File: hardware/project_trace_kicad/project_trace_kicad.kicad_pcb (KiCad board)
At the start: 4 copper layers, 100 x 100 mm, 77 parts, among them J204 Screw_Terminal_01x04, J205 Conn_Coaxial, J503 Screw_Terminal_01x04, U1 OPA2837IRUNT, U2 OPA2837IRUNT, U202 AQW280SX, U203 AQW282SX, U204 TS5A23159DGS, U206 TLE2426xLP, U301 LM358, U302 ADS1602, U304 MCP6499T, U306 LM4040DBZ-2.5, U307 LM4040DBZ-4.1, U501 UA78M33QDCYRQ1, U502 UA78M05QDCYRQ1

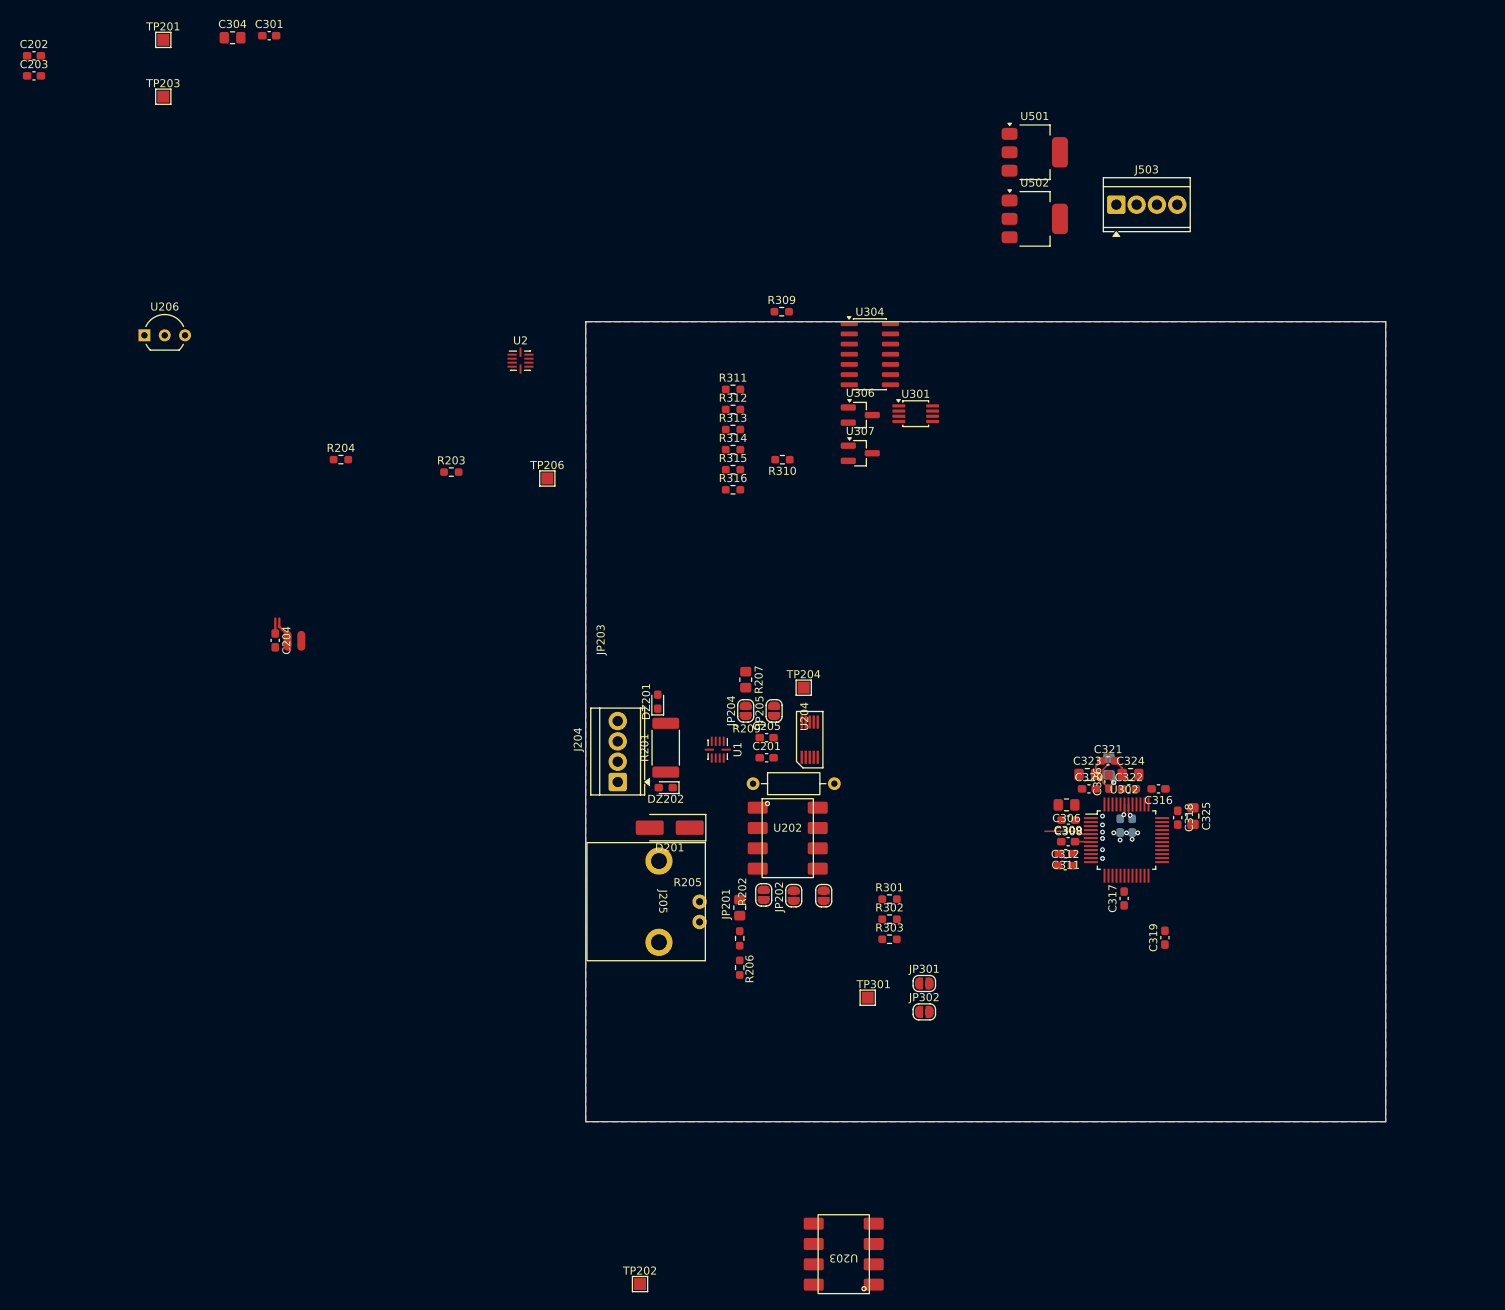
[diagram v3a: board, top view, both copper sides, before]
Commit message: Work on PCB, Fix bugs, Improve noise performance
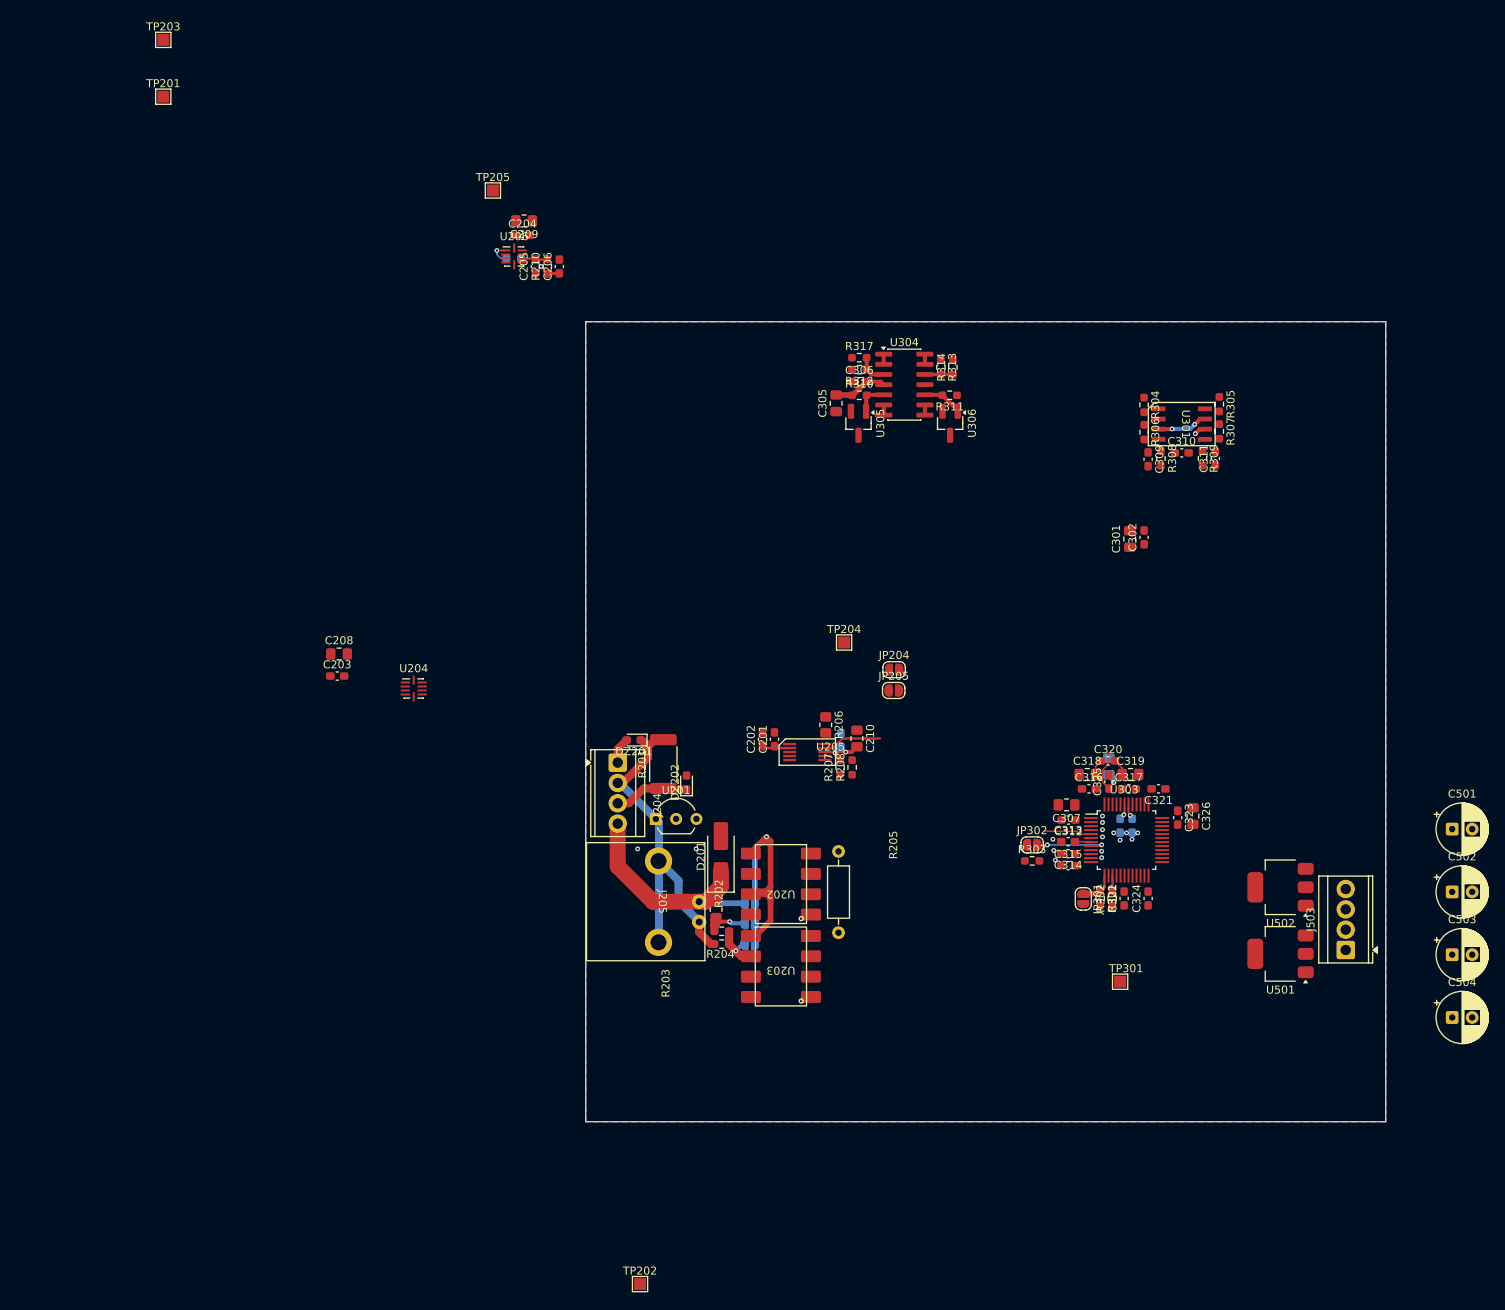
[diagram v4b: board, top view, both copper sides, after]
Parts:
- removed the R314 at (118.4, 66.0)
- removed R315: 15k, Resistor_SMD:R_0603_1608Metric_Pad0.98x0.95mm_HandSolder
- added C205: 300p, Capacitor_SMD:C_0603_1608Metric_Pad1.08x0.95mm_HandSolder, F.Cu at (93.7, 43.1)
- added C206: 680p, Capacitor_SMD:C_0603_1608Metric_Pad1.08x0.95mm_HandSolder, F.Cu at (96.7, 43.1)
- added C208: 10u, Capacitor_SMD:C_0805_2012Metric_Pad1.18x1.45mm_HandSolder, F.Cu at (69.2, 91.5)
- added C209: 10u, Capacitor_SMD:C_0805_2012Metric_Pad1.18x1.45mm_HandSolder, F.Cu at (92.3, 37.4)
- added C210: 10u, Capacitor_SMD:C_0805_2012Metric_Pad1.18x1.45mm_HandSolder, F.Cu at (133.9, 102.1)
- added C302: 100n, Capacitor_SMD:C_0603_1608Metric_Pad1.08x0.95mm_HandSolder, F.Cu at (169.8, 77.0)
- added C306: 100n, Capacitor_SMD:C_0603_1608Metric_Pad1.08x0.95mm_HandSolder, F.Cu at (134.2, 57.5)
- added C309: 100p, Capacitor_SMD:C_0603_1608Metric_Pad1.08x0.95mm_HandSolder, F.Cu at (170.3, 67.2)
- added C310: 100p, Capacitor_SMD:C_0603_1608Metric_Pad1.08x0.95mm_HandSolder, F.Cu at (174.5, 66.4)
- added C311: 100p, Capacitor_SMD:C_0603_1608Metric_Pad1.08x0.95mm_HandSolder, F.Cu at (178.7, 67.1)
- added C501: 100u, Capacitor_THT:CP_Radial_D6.3mm_P2.50mm, F.Cu at (208.3, 113.4)
- added C502: 100u, Capacitor_THT:CP_Radial_D6.3mm_P2.50mm, F.Cu at (208.3, 121.3)
- added C503: 100u, Capacitor_THT:CP_Radial_D6.3mm_P2.50mm, F.Cu at (208.3, 129.1)
- added C504: 100u, Capacitor_THT:CP_Radial_D6.3mm_P2.50mm, F.Cu at (208.3, 137.0)
- added R209: 111R, Resistor_SMD:R_0603_1608Metric_Pad0.98x0.95mm_HandSolder, B.Cu at (91.0, 42.1)
- added R210: 193R, Resistor_SMD:R_0603_1608Metric_Pad0.98x0.95mm_HandSolder, F.Cu at (95.2, 43.1)
- added R304: 330R, Resistor_SMD:R_0603_1608Metric_Pad0.98x0.95mm_HandSolder, F.Cu at (169.8, 60.4)
- added R305: 330R, Resistor_SMD:R_0603_1608Metric_Pad0.98x0.95mm_HandSolder, F.Cu at (179.2, 60.3)
- added R306: 1k, Resistor_SMD:R_0603_1608Metric_Pad0.98x0.95mm_HandSolder, F.Cu at (169.8, 63.8)
- added R307: 1k, Resistor_SMD:R_0603_1608Metric_Pad0.98x0.95mm_HandSolder, F.Cu at (179.2, 63.7)
- added R308: 24R9, Resistor_SMD:R_0603_1608Metric_Pad0.98x0.95mm_HandSolder, F.Cu at (171.9, 67.1)
- added R309: 24R9, Resistor_SMD:R_0603_1608Metric_Pad0.98x0.95mm_HandSolder, F.Cu at (177.1, 67.1)
- C207: renamed from C204; moved to B.Cu
- C301: value 100n -> 10u; footprint Capacitor_SMD:C_0603_1608Metric_Pad1.08x0.95mm_HandSolder -> Capacitor_SMD:C_0805_2012Metric_Pad1.18x1.45mm_HandSolder
- JP201, JP202, JP203: moved to B.Cu
- R207: renamed from R203; value 10k -> 1k
- R208: renamed from R204; value 89k8 -> 8k98
- U301: value LM358 -> THS4131IDR; footprint Package_SO:MSOP-8_3x3mm_P0.65mm -> ProjectTraceFootprints:SOIC8 - D0008A - THS4131IDR
- moved C301 124.6 mm to (168.0, 77.2), turned to 90 degrees
- moved U501 104.8 mm to (186.8, 129.0), turned to 180 degrees
- moved J503 97.5 mm to (195.0, 128.5), turned to 90 degrees
- moved U502 89.0 mm to (186.8, 120.7), turned to 180 degrees
- moved C305 88.2 mm to (131.3, 60.2), turned to 90 degrees
- moved U201 88.0 mm to (108.8, 112.2)
- moved C203 84.1 mm to (68.9, 94.3)
- moved R208 74.6 mm to (133.3, 105.7), turned to 90 degrees
- moved C207 71.8 mm to (131.9, 102.3), turned to 90 degrees
- moved C204 65.1 mm to (92.1, 39.2)
- moved R207 61.0 mm to (131.8, 105.7), turned to 90 degrees
- moved U204 38.8 mm to (78.5, 95.8), turned to 0 degrees
- moved U203 36.8 mm to (124.4, 130.6)
- moved TP205 36.6 mm to (88.4, 33.6)
- moved U301 33.3 mm to (174.5, 62.8)
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- renumbered C205 to C201, C201 to C202, C202 to C204, C303 to C304, C304 to C305, C306 to C307, C307 to C308, C308 to C312, C309 to C313, C311 to C314, C312 to C315, C320 to C316, C322 to C317, C323 to C318, C324 to C319, C321 to C320, C316 to C321, C317 to C322, C318 to C323, C319 to C324, C326 to C325, C325 to C326, JP302 to JP301, JP301 to JP302, R205 to R203, R206 to R204, R209 to R205, R207 to R206, R303 to R301, R301 to R302, R302 to R303, R309 to R310, R310 to R311, R313 to R312, R312 to R313, R311 to R314, R316 to R317, TP203 to TP201, TP201 to TP203, TP206 to TP205, U206 to U201, U1 to U204, U204 to U205, U2 to U206, U302 to U303, U306 to U305, U307 to U306
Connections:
- J204 pad 1: /Inputs/Voltmeter.In -> GND
- J204 pad 2: /Inputs/Ammeter.In -> VCOM
- J204 pad 3: VCOM -> /Inputs/Ammeter.In
- J204 pad 4: GND -> /Inputs/Voltmeter.In
- R311 pad 2: Net-(U301A-+) -> Net-(U304C-+)
- U202 pad 2: /Inputs/0dBAtten.~{EN} -> /Inputs/-20dBAtten.~{EN}
- U202 pad 4: /Inputs/-20dBAtten.~{EN} -> /Inputs/0dBAtten.~{EN}
- U202 pad 6: /Inputs/Attten.20dB -> /Inputs/Voltmeter.In
- U202 pad 8: /Inputs/Voltmeter.In -> /Inputs/Attten.20dB
- U203 pad 1: Net-(U202A-P1) -> GND
- U203 pad 2: /Inputs/-40dBAtten.~{EN} -> GND
- U203 pad 3: GND -> Net-(U202A-P1)
- U203 pad 4: GND -> /Inputs/-40dBAtten.~{EN}
- U203 pad 5: GND -> Net-(JP201-B)
- U203 pad 6: GND -> /Inputs/Attten.40dB
- U203 pad 7: Net-(JP201-B) -> GND
- U203 pad 8: /Inputs/Attten.40dB -> GND
- U301 pad 1: 4V1 -> Net-(R304-Pad2)
- U301 pad 2: 4V1 -> +2V5
- U301 pad 3: Net-(U301A-+) -> +5V
- U301 pad 4: GND -> Net-(R306-Pad2)
- U301 pad 5: GND -> Net-(R307-Pad2)
- U301 pad 7: unconnected-(U301-Pad7) -> +5V
- U301 pad 8: +5V -> Net-(R305-Pad2)
- U303 pad 4: GND -> Net-(U303A-AINN)
- U303 pad 5: /ADC/Signal.In -> Net-(U303A-AINP)
- U304 pad 8: +1V5 -> 4V1
- U304 pad 9: +1V5 -> 4V1
- U306 pad 1: Net-(U301A-+) -> Net-(U304C-+)
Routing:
- net VCOM: track 0.00 -> 46.3 mm
- net Net-(JP201-B): track 0.00 -> 36.7 mm, vias 0 -> 1
- net /Inputs/Voltmeter.In: track 0.00 -> 30.7 mm
- net +5V: track 5.33 -> 22.7 mm, vias 1 -> 5
- net Net-(JP302-B): track 0.00 -> 9.46 mm, vias 0 -> 2
- net /Inputs/Ammeter.In: track 0.00 -> 9.26 mm
- net /Inputs/Attten.40dB: track 0.00 -> 6.41 mm, vias 0 -> 1
- net /Inputs/Attten.20dB: track 0.00 -> 6.19 mm, vias 0 -> 1
- net Net-(U303A-AINP): track 0.00 -> 5.89 mm
- net /ADC/Signal.In: track 5.89 -> 0.00 mm
- net Net-(C206-Pad1): track 0.00 -> 5.68 mm, vias 0 -> 1
- net GND: track 0.00 -> 4.72 mm, vias 11 -> 17
- net Net-(U304C-+): track 0.00 -> 4.46 mm
- net Net-(JP301-A): track 0.00 -> 4.39 mm
- net Net-(U304B-+): track 0.00 -> 4.19 mm
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
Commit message: Layout Broad Strokes, Fix STM32H7 Error
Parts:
- added C211: 10u, Capacitor_SMD:C_0805_2012Metric_Pad1.18x1.45mm_HandSolder, F.Cu at (119.3, 119.3)
- added C212: 100n, Capacitor_SMD:C_0603_1608Metric_Pad1.08x0.95mm_HandSolder, F.Cu at (117.5, 119.5)
- added U503: NUCLEO-H753ZI, ProjectTraceFootprints:MODULE_NUCLEO-H753ZI, F.Cu at (148.2, 79.1)
- C210, C301, C302: moved to B.Cu
- moved TP201 143.1 mm to (151.2, 120.1), turned to 90 degrees
- moved TP203 129.9 mm to (124.9, 118.9), turned to 180 degrees
- moved TP205 93.1 mm to (135.7, 113.8), turned to 180 degrees
- moved C305 91.9 mm to (165.3, 145.6), turned to 180 degrees
- moved C306 89.8 mm to (162.6, 142.7), turned to 90 degrees
- moved R209 89.4 mm to (137.7, 118.3)
- moved C206 89.4 mm to (143.4, 119.3)
- moved C204 89.3 mm to (138.7, 115.4)
- moved C209 89.3 mm to (138.9, 113.6)
- moved U206 89.3 mm to (137.6, 118.0)
- moved C205 89.3 mm to (140.3, 119.3)
- moved R210 89.3 mm to (141.8, 119.3)
- moved R310 88.7 mm to (164.3, 142.7), turned to 90 degrees
- moved R313 88.7 mm to (161.1, 142.8), turned to 90 degrees
- moved R314 88.2 mm to (159.6, 142.8)
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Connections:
- R206 pad 2: Net-(JP204-B) -> Net-(JP205-A)
- R312 pad 1: Net-(U304A-+) -> Net-(U304D-+)
- R313 pad 2: Net-(U304D-+) -> Net-(U304A-+)
- R314 pad 1: Net-(U304D-+) -> Net-(U304A-+)
- R317 pad 2: Net-(U304A-+) -> Net-(U304D-+)
- U205 pad 1: /Inputs/ACCouple.EN -> /Inputs/20dBGain.EN
- U205 pad 10: Net-(JP204-B) -> Net-(R209-Pad1)
- U205 pad 2: /Inputs/AttenBuffer -> Net-(R208-Pad1)
- U205 pad 4: Net-(R208-Pad1) -> /Inputs/AttenBuffer
- U205 pad 5: /Inputs/20dBGain.EN -> /Inputs/ACCouple.EN
- U205 pad 6: Net-(R209-Pad1) -> Net-(JP204-B)
- U205 pad 7: Net-(U206A--) -> Net-(JP205-A)
- U205 pad 9: Net-(JP205-A) -> Net-(U206A--)
- U304 pad 1: +4V -> +1V0
- U304 pad 13: +1V0 -> +4V
- U304 pad 14: +1V0 -> +4V
- U304 pad 2: +4V -> +1V0
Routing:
- net +3V3: track 0.00 -> 38.8 mm, vias 0 -> 2
- net Net-(J503-Pin_1): track 0.00 -> 35.5 mm
- net +5V: track 22.7 -> 55.6 mm, vias 5 -> 8
- net Net-(U202A-P1): track 0.00 -> 18.4 mm
- net GND: track 4.72 -> 22.4 mm, vias 17 -> 82
- net Net-(JP204-B): track 0.00 -> 17.6 mm
- net +2V5: track 8.56 -> 25.8 mm
- net /Inputs/AttenBuffer: track 3.50 -> 16.9 mm
- net Net-(U206A--): track 0.00 -> 11.0 mm
- net /Inputs/Ammeter.In: track 9.26 -> 20.2 mm
- net /Inputs/Attten.20dB: track 6.19 -> 16.2 mm, vias 1 -> 2
- net 4V1: track 1.27 -> 10.5 mm
- net /ADC/Signal.In: track 0.00 -> 8.42 mm
- net +4V: track 3.35 -> 11.1 mm
- net +1V0: track 3.57 -> 10.8 mm
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
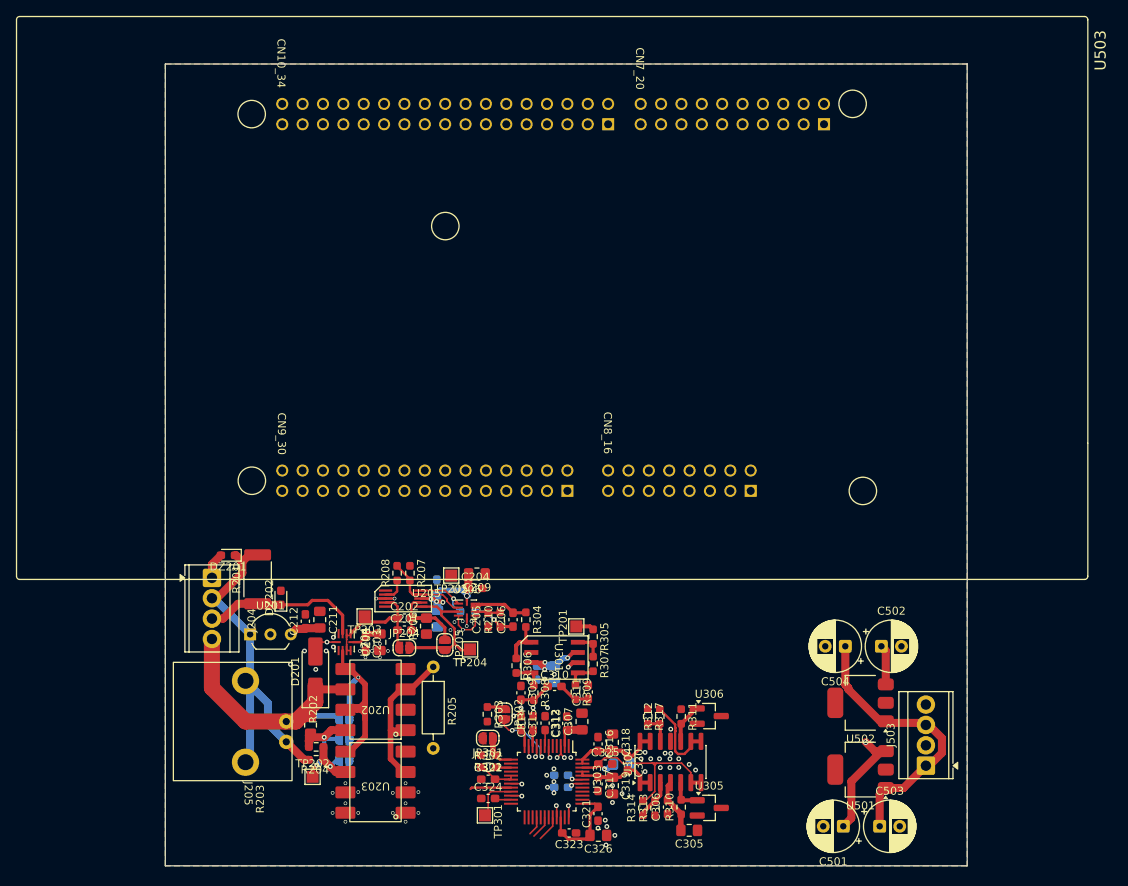
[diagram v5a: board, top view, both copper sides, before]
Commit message: Add missing Part-numers, Revise AC Coupling
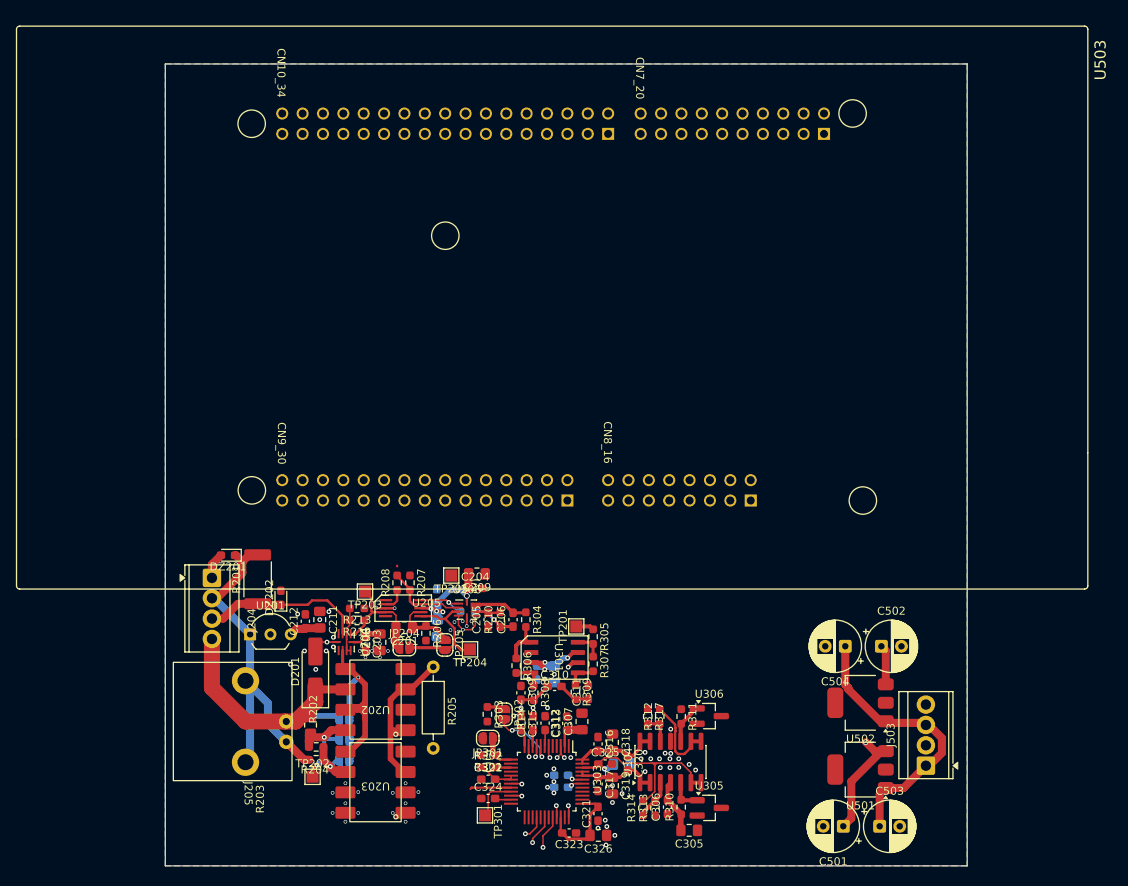
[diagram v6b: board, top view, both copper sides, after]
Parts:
- removed C202: 3n3, Capacitor_SMD:C_0603_1608Metric_Pad1.08x0.95mm_HandSolder
- added R212: 1k, Resistor_SMD:R_0603_1608Metric_Pad0.98x0.95mm_HandSolder, F.Cu at (123.9, 119.4)
- added R213: 193R, Resistor_SMD:R_0603_1608Metric_Pad0.98x0.95mm_HandSolder, F.Cu at (123.9, 117.9)
- C201: value 3n3 -> 10u; footprint Capacitor_SMD:C_0603_1608Metric_Pad1.08x0.95mm_HandSolder -> Capacitor_SMD:C_0805_2012Metric_Pad1.18x1.45mm_HandSolder
- R206: value 1M8 -> 10k; footprint Resistor_SMD:R_0805_2012Metric_Pad1.20x1.40mm_HandSolder -> Resistor_SMD:R_0603_1608Metric_Pad0.98x0.95mm_HandSolder
- moved TP203 3.10 mm to (124.9, 115.8)
- moved C207 1.20 mm to (133.9, 116.4)
- moved C210 1.20 mm to (133.9, 120.4)
- moved R207 1.20 mm to (130.5, 114.7)
- moved R208 1.20 mm to (128.9, 114.7)
- moved U205 1.20 mm to (129.7, 117.9)
- moved U503 1.20 mm to (148.2, 80.3)
- moved R206 0.90 mm to (132.5, 121.0), turned to -90 degrees
- moved C201 0.30 mm to (129.8, 120.3), turned to 180 degrees
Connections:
- net /Inputs/ACCouple.EN renamed /Inputs/ACCouple.~{EN}
- C201 pad 1: /Inputs/AttenBuffer -> Net-(JP205-A)
- C201 pad 2: Net-(JP205-A) -> /Inputs/AttenBuffer
- R206 pad 1: VCOM -> Net-(JP205-A)
- R206 pad 2: Net-(JP205-A) -> VCOM
- U204 pad 2: /Inputs/AttenBuffer -> Net-(U204A--)
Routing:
- net Net-(JP205-A): track 10.6 -> 7.85 mm
- net Net-(U204A--): track 0.00 -> 2.77 mm
- net Net-(R209-Pad1): track 7.83 -> 6.81 mm
- net /ADC/FSO: track 3.29 -> 4.25 mm, vias 0 -> 1
- net /Inputs/AttenBuffer: track 16.9 -> 17.8 mm
- net Net-(JP204-B): track 17.6 -> 16.7 mm
- net /ADC/DOUT: track 2.91 -> 3.78 mm, vias 0 -> 1
- net Net-(U206A--): track 11.0 -> 10.4 mm
- net /ADC/SCLK: track 2.40 -> 2.96 mm, vias 0 -> 1
- net GND: track 22.4 -> 22.5 mm, vias 82 -> 85
